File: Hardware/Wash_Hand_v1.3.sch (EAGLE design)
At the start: 63 parts, among them IC1 LM358D, IC2 LP298XS, IC3 405016TSSOP, J1 I2C, J2 ICSP, J3 SPI, J4 9V_CONN, J5 EXT_VCC, J6 6_PIN_SERIAL_CABLEPTH, Q1 16.0 Mhz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

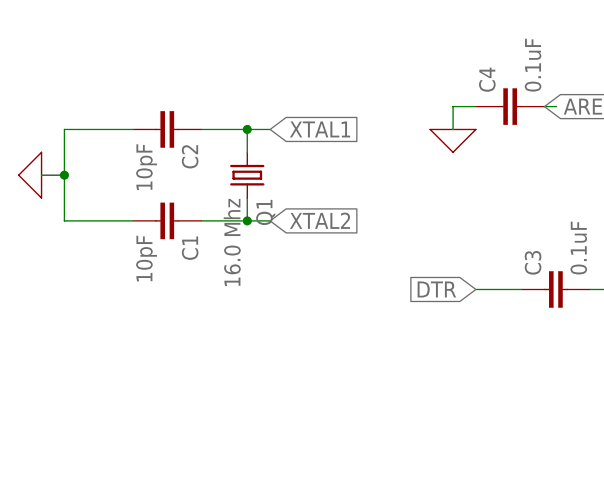
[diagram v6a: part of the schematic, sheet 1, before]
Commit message: Board/Schematic: Add 1M resistor between capacitors (crystal) and move the capacitors
To make it easier to put on the board.

Signed-off-by: Konrad Rzeszutek Wilk <konrad@kernel.org>
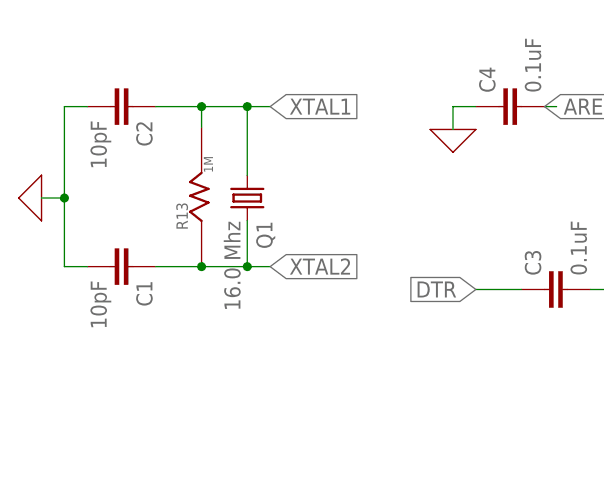
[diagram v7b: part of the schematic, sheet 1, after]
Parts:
- added R13: 1M, darnok_common:RESISTORR1206
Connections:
- net XTAL1: now also R13.R_2
- net XTAL2: now also R13.R_1
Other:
- moved on the sheet: C1, C2, Q1
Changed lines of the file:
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@@
 <part name="X_28" library="ngspice-simulation" library_urn="urn:adsk.eagle:library:527439" deviceset="GND" device=""/>
 <part name="R12" library="darnok_common" deviceset="RESISTOR" device="R1206" value="1K"/>
+<part name="R13" library="darnok_common" deviceset="RESISTOR" device="R1206" value="1M"/>
 </parts>
 <sheets>
@@
 </plain>
 <instances>
-<instance part="Q1" gate="G$1" x="33.02" y="187.96" smashed="yes" rot="R270">
-<attribute name="NAME" x="34.036" y="185.42" size="1.778" layer="95" rot="R270"/>
-<attribute name="VALUE" x="30.48" y="185.42" size="1.778" layer="96" rot="R270"/>
-</instance>
-<instance part="C1" gate="G$1" x="22.86" y="182.88" smashed="yes" rot="R270">
-<attribute name="NAME" x="25.781" y="181.356" size="1.778" layer="95" font="vector" rot="R270"/>
-<attribute name="VALUE" x="20.701" y="181.356" size="1.778" layer="96" font="vector" rot="R270"/>
-</instance>
-<instance part="C2" gate="G$1" x="22.86" y="193.04" smashed="yes" rot="R270">
-<attribute name="NAME" x="25.781" y="191.516" size="1.778" layer="95" font="vector" rot="R270"/>
-<attribute name="VALUE" x="20.701" y="191.516" size="1.778" layer="96" font="vector" rot="R270"/>
+<instance part="Q1" gate="G$1" x="33.02" y="185.42" smashed="yes" rot="R270">
+<attribute name="NAME" x="34.036" y="182.88" size="1.778" layer="95" rot="R270"/>
+<attribute name="VALUE" x="30.48" y="182.88" size="1.778" layer="96" rot="R270"/>
+</instance>
+<instance part="C1" gate="G$1" x="17.78" y="177.8" smashed="yes" rot="R270">
+<attribute name="NAME" x="20.701" y="176.276" size="1.778" layer="95" font="vector" rot="R270"/>
+<attribute name="VALUE" x="15.621" y="176.276" size="1.778" layer="96" font="vector" rot="R270"/>
+</instance>
+<instance part="C2" gate="G$1" x="17.78" y="195.58" smashed="yes" rot="R270">
+<attribute name="NAME" x="20.701" y="194.056" size="1.778" layer="95" font="vector" rot="R270"/>
+<attribute name="VALUE" x="15.621" y="194.056" size="1.778" layer="96" font="vector" rot="R270"/>
 </instance>
 <instance part="U$5" gate="G$1" x="210.82" y="76.2" smashed="yes">
@@
 <attribute name="VALUE" x="93.98" y="180.34" size="1.27" layer="96" rot="R90"/>
 </instance>
-<instance part="X_3" gate="G$1" x="10.16" y="187.96" smashed="yes" rot="R270"/>
+<instance part="X_3" gate="G$1" x="10.16" y="185.42" smashed="yes" rot="R270"/>
 <instance part="J1" gate="G$1" x="154.94" y="198.12" smashed="yes" rot="R180">
 <attribute name="VALUE" x="157.48" y="202.946" size="1.778" layer="96" font="vector" rot="R180"/>
@@
 <attribute name="NAME" x="77.216" y="161.544" size="1.27" layer="95" rot="R90"/>
 <attribute name="VALUE" x="80.01" y="167.894" size="1.016" layer="96" rot="R90"/>
+</instance>
+<instance part="R13" gate="G$1" x="27.94" y="182.88" smashed="yes" rot="R90">
+<attribute name="NAME" x="26.416" y="181.864" size="1.27" layer="95" rot="R90"/>
+<attribute name="VALUE" x="29.21" y="188.214" size="1.016" layer="96" rot="R90"/>
 </instance>
 </instances>
@@
 <segment>
 <pinref part="X_3" gate="G$1" pin="0"/>
-<wire x1="10.16" y1="187.96" x2="12.7" y2="187.96" width="0.1524" layer="91"/>
-<junction x="12.7" y="187.96"/>
-<wire x1="12.7" y1="187.96" x2="12.7" y2="193.04" width="0.1524" layer="91"/>
+<wire x1="10.16" y1="185.42" x2="12.7" y2="185.42" width="0.1524" layer="91"/>
+<junction x="12.7" y="185.42"/>
+<wire x1="12.7" y1="185.42" x2="12.7" y2="195.58" width="0.1524" layer="91"/>
 <pinref part="C2" gate="G$1" pin="2"/>
-<wire x1="12.7" y1="193.04" x2="20.32" y2="193.04" width="0.1524" layer="91"/>
+<wire x1="12.7" y1="195.58" x2="15.24" y2="195.58" width="0.1524" layer="91"/>
 <pinref part="C1" gate="G$1" pin="2"/>
-<wire x1="20.32" y1="182.88" x2="12.7" y2="182.88" width="0.1524" layer="91"/>
-<wire x1="12.7" y1="182.88" x2="12.7" y2="187.96" width="0.1524" layer="91"/>
+<wire x1="15.24" y1="177.8" x2="12.7" y2="177.8" width="0.1524" layer="91"/>
+<wire x1="12.7" y1="177.8" x2="12.7" y2="185.42" width="0.1524" layer="91"/>
 </segment>
 <segment>
@@
 <segment>
 <pinref part="Q1" gate="G$1" pin="2"/>
-<wire x1="33.02" y1="182.88" x2="33.02" y2="185.42" width="0.1524" layer="91"/>
-<wire x1="33.02" y1="182.88" x2="35.56" y2="182.88" width="0.1524" layer="91"/>
-<label x="35.56" y="182.88" size="1.778" layer="95" xref="yes"/>
+<wire x1="33.02" y1="177.8" x2="33.02" y2="182.88" width="0.1524" layer="91"/>
+<wire x1="33.02" y1="177.8" x2="35.56" y2="177.8" width="0.1524" layer="91"/>
+<label x="35.56" y="177.8" size="1.778" layer="95" xref="yes"/>
 <pinref part="C1" gate="G$1" pin="1"/>
-<wire x1="27.94" y1="182.88" x2="33.02" y2="182.88" width="0.1524" layer="91"/>
-<junction x="33.02" y="182.88"/>
+<wire x1="22.86" y1="177.8" x2="27.94" y2="177.8" width="0.1524" layer="91"/>
+<junction x="33.02" y="177.8"/>
+<pinref part="R13" gate="G$1" pin="R_1"/>
+<wire x1="27.94" y1="177.8" x2="33.02" y2="177.8" width="0.1524" layer="91"/>
+<junction x="27.94" y="177.8"/>
 </segment>
 <segment>
@@
 <segment>
 <pinref part="Q1" gate="G$1" pin="1"/>
-<wire x1="33.02" y1="193.04" x2="33.02" y2="190.5" width="0.1524" layer="91"/>
-<wire x1="33.02" y1="193.04" x2="35.56" y2="193.04" width="0.1524" layer="91"/>
-<label x="35.56" y="193.04" size="1.778" layer="95" xref="yes"/>
-<junction x="33.02" y="193.04"/>
+<wire x1="33.02" y1="195.58" x2="33.02" y2="187.96" width="0.1524" layer="91"/>
+<wire x1="33.02" y1="195.58" x2="35.56" y2="195.58" width="0.1524" layer="91"/>
+<label x="35.56" y="195.58" size="1.778" layer="95" xref="yes"/>
 <pinref part="C2" gate="G$1" pin="1"/>
-<wire x1="33.02" y1="193.04" x2="27.94" y2="193.04" width="0.1524" layer="91"/>
-</segment>
-<segment>
+<wire x1="22.86" y1="195.58" x2="27.94" y2="195.58" width="0.1524" layer="91"/>
+<junction x="33.02" y="195.58"/>
+<junction x="27.94" y="195.58"/>
+<wire x1="27.94" y1="195.58" x2="33.02" y2="195.58" width="0.1524" layer="91"/>
+<pinref part="R13" gate="G$1" pin="R_2"/>
+<wire x1="27.94" y1="193.294" x2="27.94" y2="195.58" width="0.1524" layer="91"/>
+</segment>
+<segment>

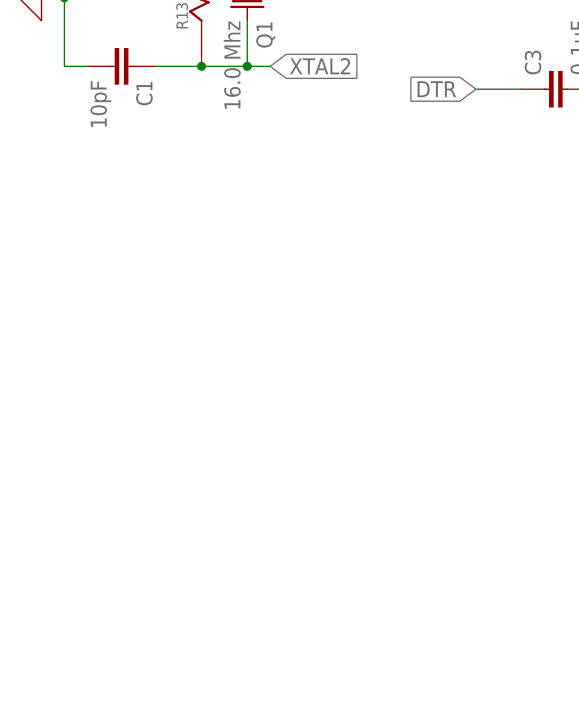
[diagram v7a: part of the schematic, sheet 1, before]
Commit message: Board/Schematic: Add resonator (on top of crystal)
So that we can use either the resonator or
the crystal+capacitor.

Signed-off-by: Konrad Rzeszutek Wilk <konrad@kernel.org>
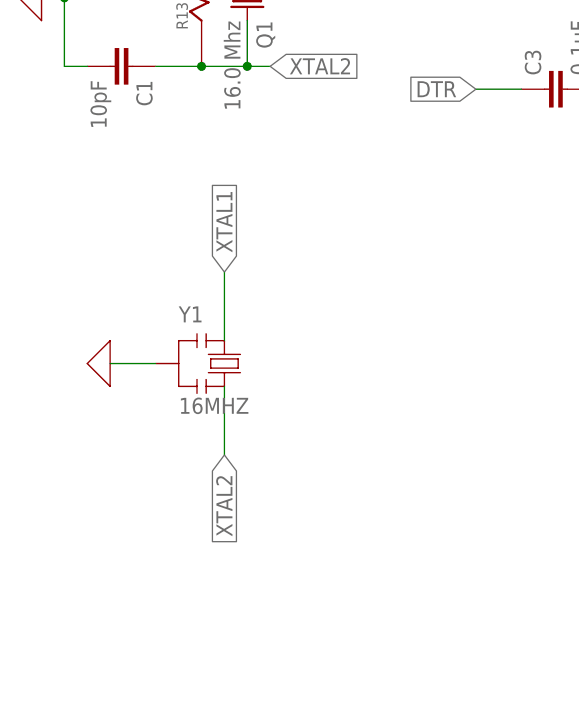
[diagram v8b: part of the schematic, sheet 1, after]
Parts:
- added Y1: 16MHZ, darnok_common:RESONATORMU
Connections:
- net 0: now also Y1.2
- net XTAL1: now also Y1.1
- net XTAL2: now also Y1.3
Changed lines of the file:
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@@
 <part name="R12" library="darnok_common" deviceset="RESISTOR" device="R1206" value="1K"/>
 <part name="R13" library="darnok_common" deviceset="RESISTOR" device="R1206" value="1M"/>
+<part name="Y1" library="darnok_common" deviceset="RESONATOR" device="MU" value="16MHZ"/>
+<part name="X_29" library="ngspice-simulation" library_urn="urn:adsk.eagle:library:527439" deviceset="GND" device=""/>
 </parts>
 <sheets>
@@
 <attribute name="VALUE" x="29.21" y="188.214" size="1.016" layer="96" rot="R90"/>
 </instance>
+<instance part="Y1" gate="G$1" x="30.48" y="144.78" smashed="yes">
+<attribute name="NAME" x="25.4" y="149.352" size="1.778" layer="95"/>
+<attribute name="VALUE" x="25.4" y="139.192" size="1.778" layer="96"/>
+</instance>
+<instance part="X_29" gate="G$1" x="17.78" y="144.78" smashed="yes" rot="R270"/>
 </instances>
 <busses>
@@
 <pinref part="R12" gate="G$1" pin="R_1"/>
 </segment>
+<segment>
+<pinref part="Y1" gate="G$1" pin="2"/>
+<wire x1="22.86" y1="144.78" x2="17.78" y2="144.78" width="0.1524" layer="91"/>
+<pinref part="X_29" gate="G$1" pin="0"/>
+</segment>
 </net>
 <net name="D0" class="0">
@@
 <label x="134.62" y="127" size="1.778" layer="95" rot="R180" xref="yes"/>
 <pinref part="U2" gate="U$1" pin="PB7(XTAL2/TOSC2)"/>
+</segment>
+<segment>
+<pinref part="Y1" gate="G$1" pin="3"/>
+<wire x1="30.48" y1="142.24" x2="30.48" y2="134.62" width="0.1524" layer="91"/>
+<label x="30.48" y="134.62" size="1.778" layer="95" rot="R270" xref="yes"/>
 </segment>
 </net>
@@
 <pinref part="U2" gate="U$1" pin="PB6(XTAL1/TOSC1)"/>
 </segment>
-</net>
+<segment>
+<pinref part="Y1" gate="G$1" pin="1"/>
+<wire x1="30.48" y1="147.32" x2="30.48" y2="154.94" width="0.1524" layer="91"/>
+<label x="30.48" y="154.94" size="1.778" layer="95" rot="R90" xref="yes"/>
+</segment>
+</net>
